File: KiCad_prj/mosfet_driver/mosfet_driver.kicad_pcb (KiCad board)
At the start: 2 copper layers, 75 x 40 mm, 62 parts, among them J1 KLS S1G03C, J2 KLS S1G03C, J3 KLS S1G03C, J4 KLS S1G02C, J5 KLS S1G02C, U1 MGJ2D051505SC, U2 MGJ2D051505SC, U3 UCC21520ADW, U4 74HC14

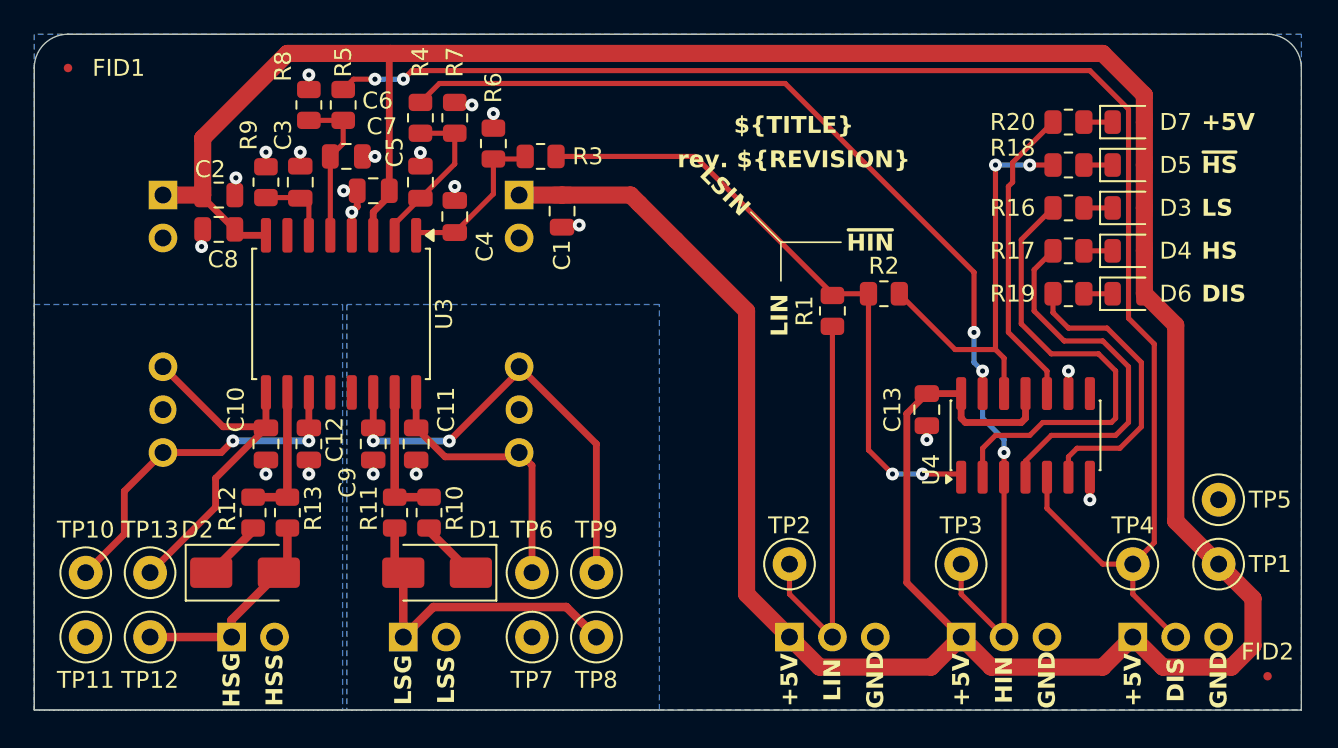
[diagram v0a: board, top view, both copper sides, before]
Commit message: Mosfet driver v rev. 1.0 odeslan do vyroby
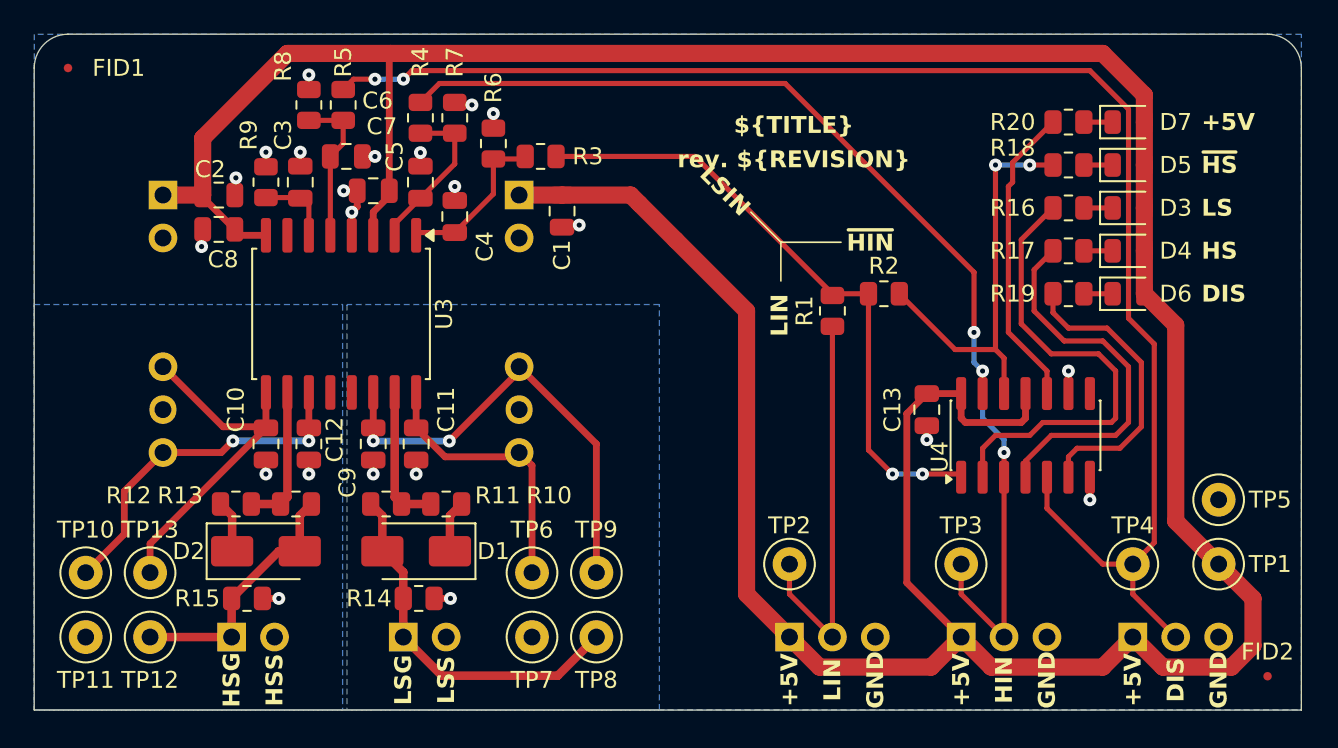
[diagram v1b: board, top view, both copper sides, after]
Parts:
- added R14: 10k, Resistor_SMD:R_0805_2012Metric, F.Cu at (125.9, 118.1)
- added R15: 10k, Resistor_SMD:R_0805_2012Metric, F.Cu at (115.7, 118.1)
- TP1, TP10, TP11, TP12, TP13, TP2, TP3, TP4, TP5, TP6, TP7, TP8, TP9: value TestPoint -> D1MM
- moved D1 1.77 mm to (125.7, 115.3)
- moved D2 1.77 mm to (116.8, 115.3)
- moved R12 1.14 mm to (115.1, 112.5), turned to 180 degrees
- moved R10 1.14 mm to (127.5, 112.5), turned to 0 degrees
- moved R11 0.72 mm to (124.0, 112.5), turned to 180 degrees
- moved R13 0.72 mm to (118.6, 112.5), turned to 0 degrees
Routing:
- net /GATEHS: track 12.6 -> 15.4 mm
- net /GATELS: track 19.6 -> 22.0 mm
- net /Driver/HS.GND: track 1.66 -> 2.63 mm, vias 2 -> 3
- net /Driver/LS.GND: track 1.66 -> 2.62 mm, vias 2 -> 3
- net /Driver/HSGATE_PULL: track 3.67 -> 3.08 mm
- net /Driver/LSGATE_PULL: track 3.67 -> 3.08 mm

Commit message: Oprava budice na zaklade vysledku zkousek, pridano drazkovani
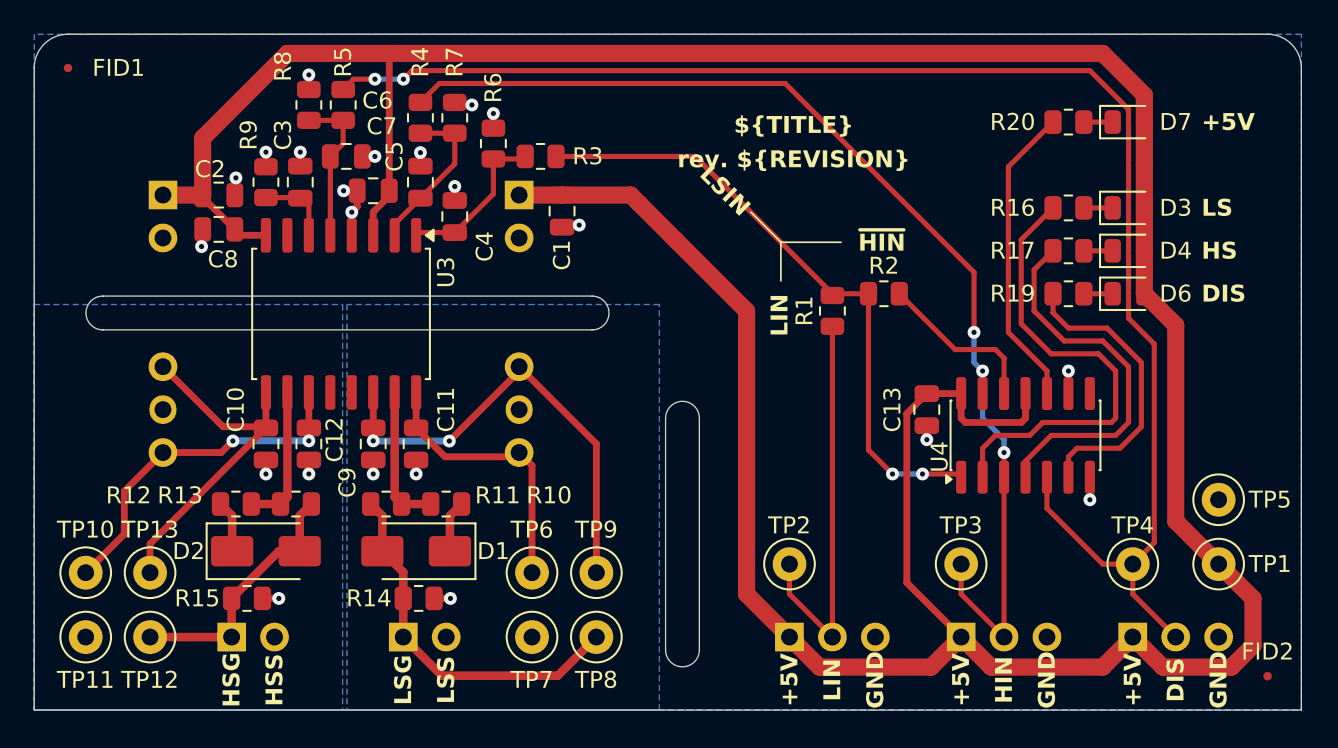
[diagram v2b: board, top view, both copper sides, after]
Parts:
- removed D5: RED, LED_SMD:LED_0805_2012Metric
- removed R18: 1k, Resistor_SMD:R_0805_2012Metric
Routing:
- net /Singnal Check/~{HSIN}: track 24.2 -> 9.87 mm, vias 2 -> 0
- net Net-(D5-K): track 1.71 -> 0.00 mm
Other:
- outline, holes or cut-outs redrawn
- board text removed: "~{HS}"
